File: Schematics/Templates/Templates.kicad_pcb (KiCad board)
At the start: 4 copper layers, 48 x 48 mm, 2 parts, among them J1 Stack Male Edge Connector, U1 SAM-M8Q

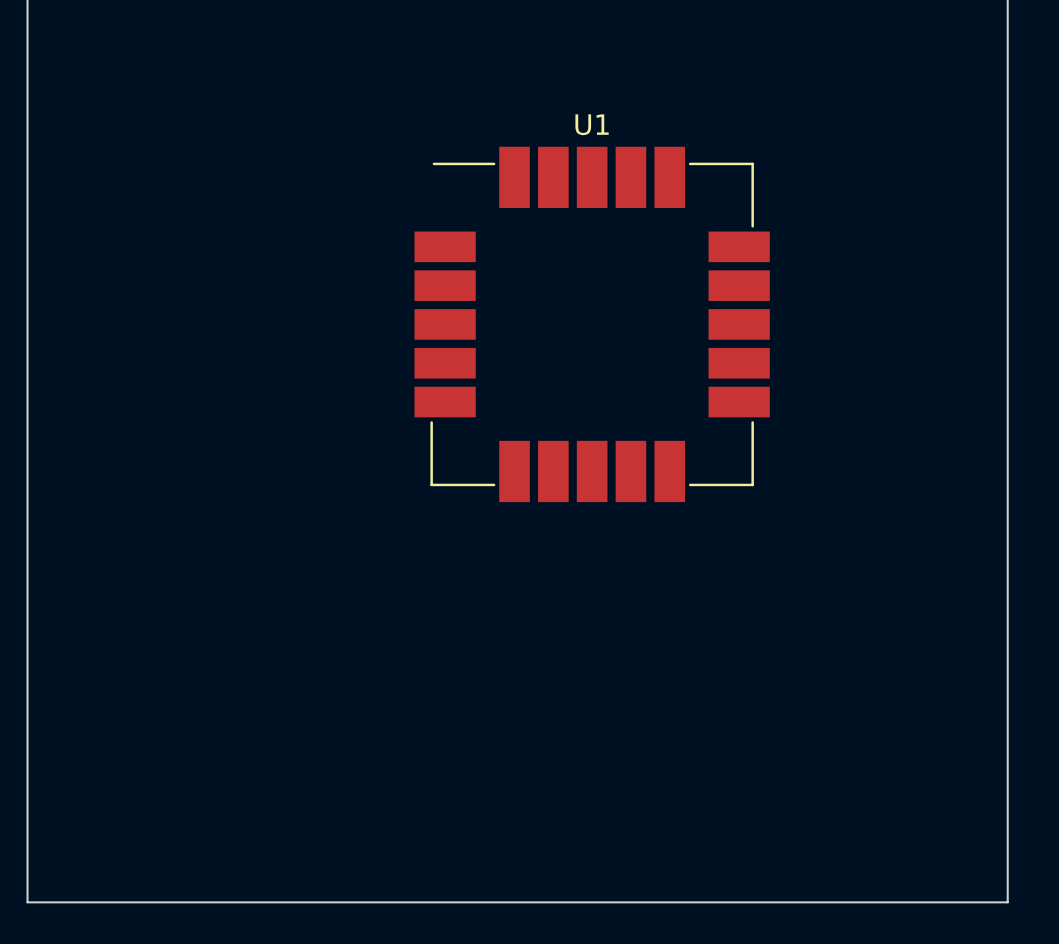
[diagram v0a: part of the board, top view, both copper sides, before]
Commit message: Added SWD programming header
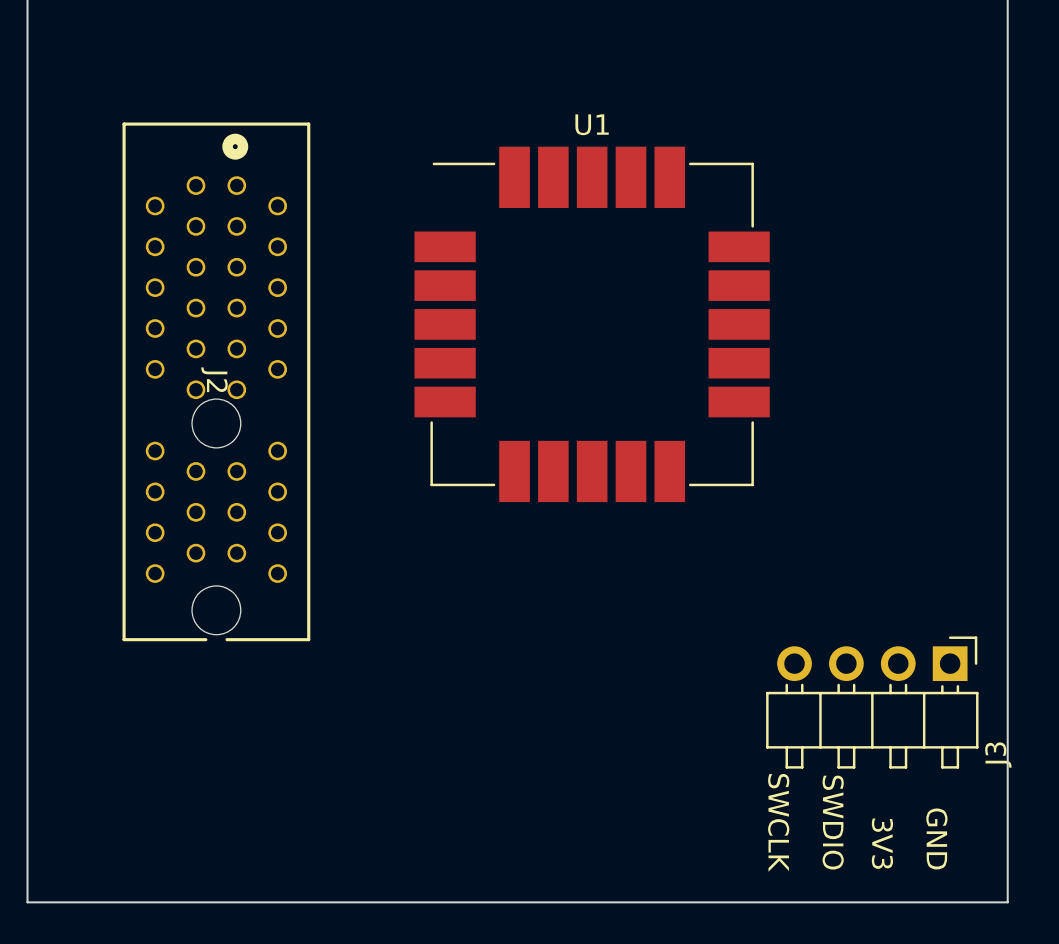
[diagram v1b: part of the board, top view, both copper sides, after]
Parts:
- added J2: Stack Female Edge Connector, footprints:CONN_10018784_AMP, F.Cu at (196.2, 101.5)
- added J3: SWD_01x04_Pin, SWD_Header:SWD_PinHeader_1x04_P2.54mm_Horizontal, F.Cu at (231.1, 124.9)
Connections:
- J1 pad A1: unconnected-(J1-~{PRSNT1}-PadA1) -> Net-(J1-BATT_A-PadA1)
- J1 pad A10: Net-(J1-+3.3V-PadA10) -> Net-(J1-BATT_B-PadA10)
- J1 pad A11: unconnected-(J1-~{PERST}-PadA11) -> Net-(J1-GND_B-PadA11)
- J1 pad A12: unconnected-(J1-GND-PadA12) -> Net-(J1-GND_B-PadA11)
- J1 pad A13: unconnected-(J1-REFCLK+-PadA13) -> Net-(J1-3.3V_B-PadA13)
- J1 pad A14: unconnected-(J1-REFCLK--PadA14) -> Net-(J1-GND_B-PadA11)
- J1 pad A15: unconnected-(J1-GND-PadA12) -> unconnected-(J1-CAN_H-PadA15)
- J1 pad A18: unconnected-(J1-GND-PadA12) -> unconnected-(J1-Reserved-PadA18)
- J1 pad A2: Net-(J1-+12V-PadA2) -> Net-(J1-BATT_A-PadA1)
- J1 pad A3: Net-(J1-+12V-PadA2) -> Net-(J1-GND_A-PadA3)
- J1 pad A4: unconnected-(J1-GND-PadA12) -> Net-(J1-GND_A-PadA3)
- J1 pad A5: unconnected-(J1-JTAG2-PadA5) -> Net-(J1-3.3V_A-PadA5)
- J1 pad A6: unconnected-(J1-JTAG3-PadA6) -> Net-(J1-GND_A-PadA3)
- J1 pad A7: unconnected-(J1-JTAG4-PadA7) -> Net-(J1-5.0V_A-PadA7)
- J1 pad A8: unconnected-(J1-JTAG5-PadA8) -> Net-(J1-GND_A-PadA3)
- J1 pad A9: Net-(J1-+3.3V-PadA10) -> Net-(J1-BATT_B-PadA10)
- J1 pad B1: Net-(J1-+12V-PadA2) -> Net-(J1-BATT_A-PadA1)
- J1 pad B10: unconnected-(J1-3.3Vaux-PadB10) -> Net-(J1-BATT_B-PadA10)
- J1 pad B11: unconnected-(J1-~{WAKE}-PadB11) -> Net-(J1-GND_B-PadA11)
- J1 pad B12: unconnected-(J1-RSVD-PadB12) -> Net-(J1-GND_B-PadA11)
- J1 pad B13: unconnected-(J1-GND-PadA12) -> Net-(J1-3.3V_B-PadA13)
- J1 pad B14: unconnected-(J1-PETp0-PadB14) -> Net-(J1-GND_B-PadA11)
- J1 pad B16: unconnected-(J1-GND-PadA12) -> unconnected-(J1-Reserved-PadB16)
- J1 pad B18: unconnected-(J1-GND-PadA12) -> unconnected-(J1-Reserved-PadB18)
- J1 pad B2: Net-(J1-+12V-PadA2) -> Net-(J1-BATT_A-PadA1)
- J1 pad B3: Net-(J1-+12V-PadA2) -> Net-(J1-GND_A-PadA3)
- J1 pad B4: unconnected-(J1-GND-PadA12) -> Net-(J1-GND_A-PadA3)
- J1 pad B5: unconnected-(J1-SMCLK-PadB5) -> Net-(J1-3.3V_A-PadA5)
- J1 pad B6: unconnected-(J1-SMDAT-PadB6) -> Net-(J1-GND_A-PadA3)
- J1 pad B7: unconnected-(J1-GND-PadA12) -> Net-(J1-5.0V_A-PadA7)
- J1 pad B8: Net-(J1-+3.3V-PadA10) -> Net-(J1-GND_A-PadA3)
- J1 pad B9: unconnected-(J1-JTAG1-PadB9) -> Net-(J1-BATT_B-PadA10)

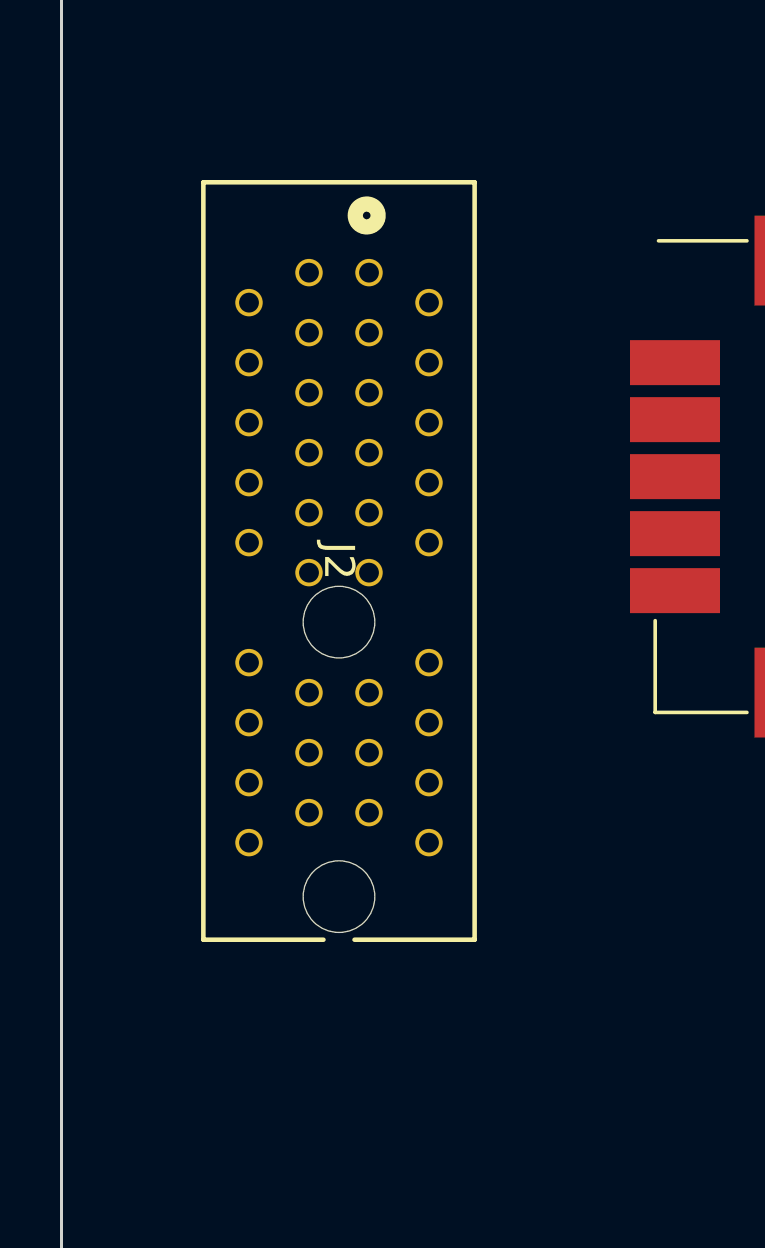
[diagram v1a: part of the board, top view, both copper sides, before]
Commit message: Updated female edge connector footprint & model
Switched to the 10018784-10210TLF PCIe 1x female connector. Updated footprint appropriately, and added 3D model.
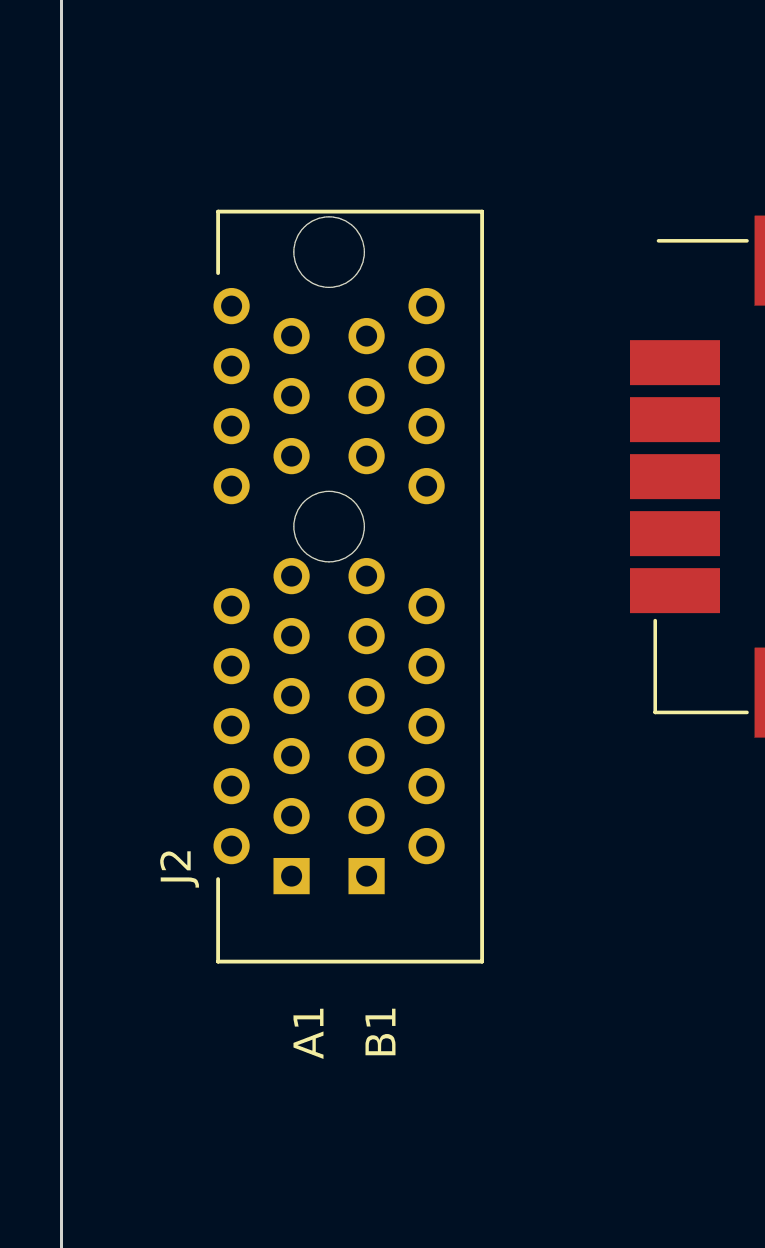
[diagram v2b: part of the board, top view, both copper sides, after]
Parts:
- J2: footprint footprints:CONN_10018784_AMP -> footprints:AMPHENOL_10018784-10210TLF
- moved J2 8.57 mm to (194.9, 110.0), turned to 90 degrees

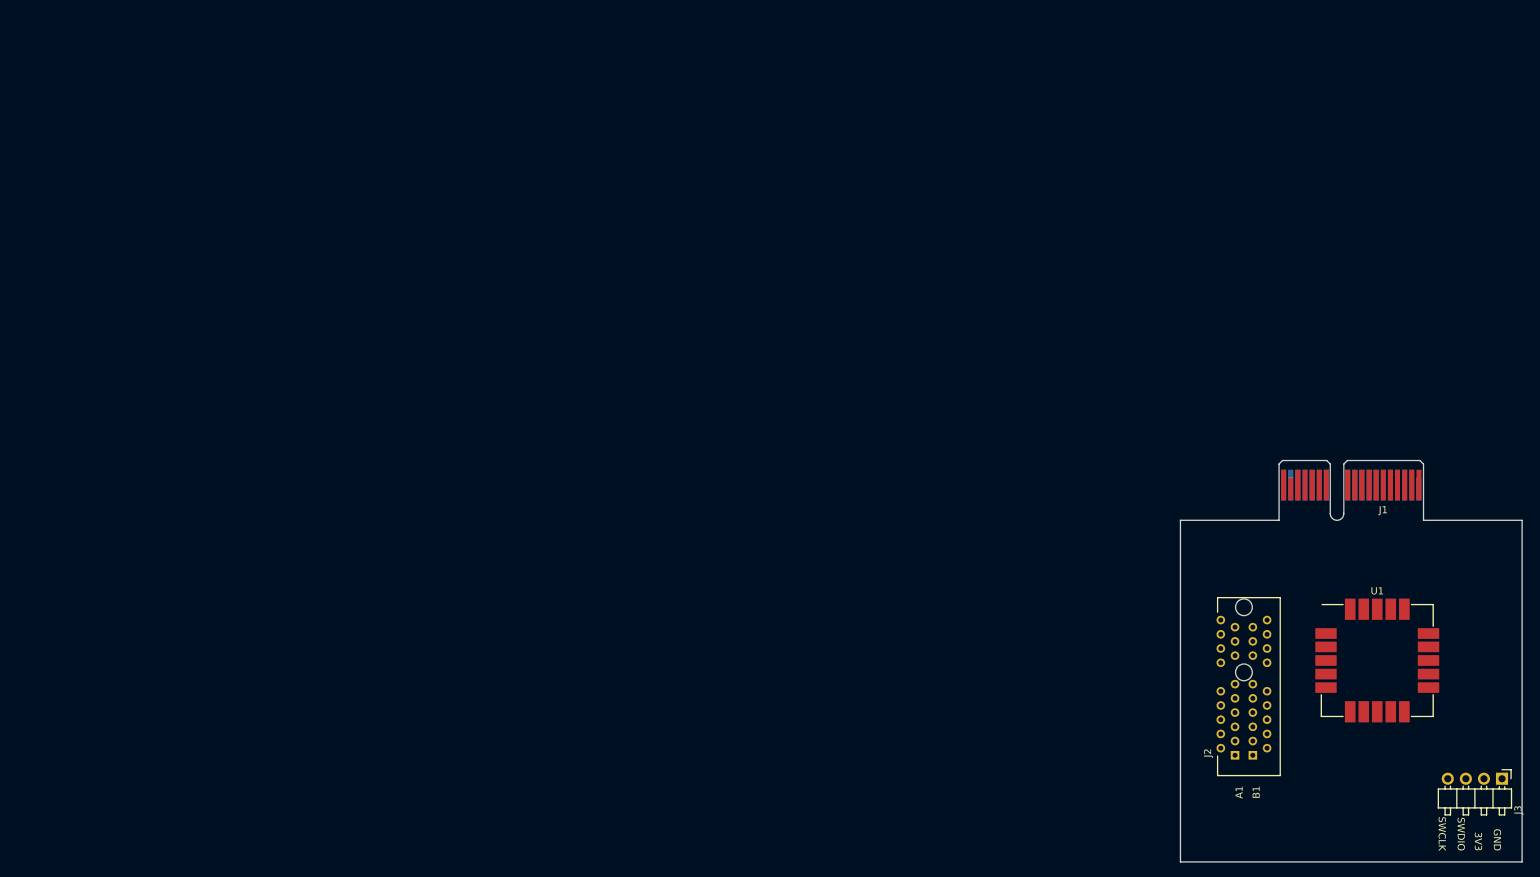
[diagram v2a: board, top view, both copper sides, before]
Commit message: Updated PCB Template
Adjusted PCB project settings & updated PCB board outline
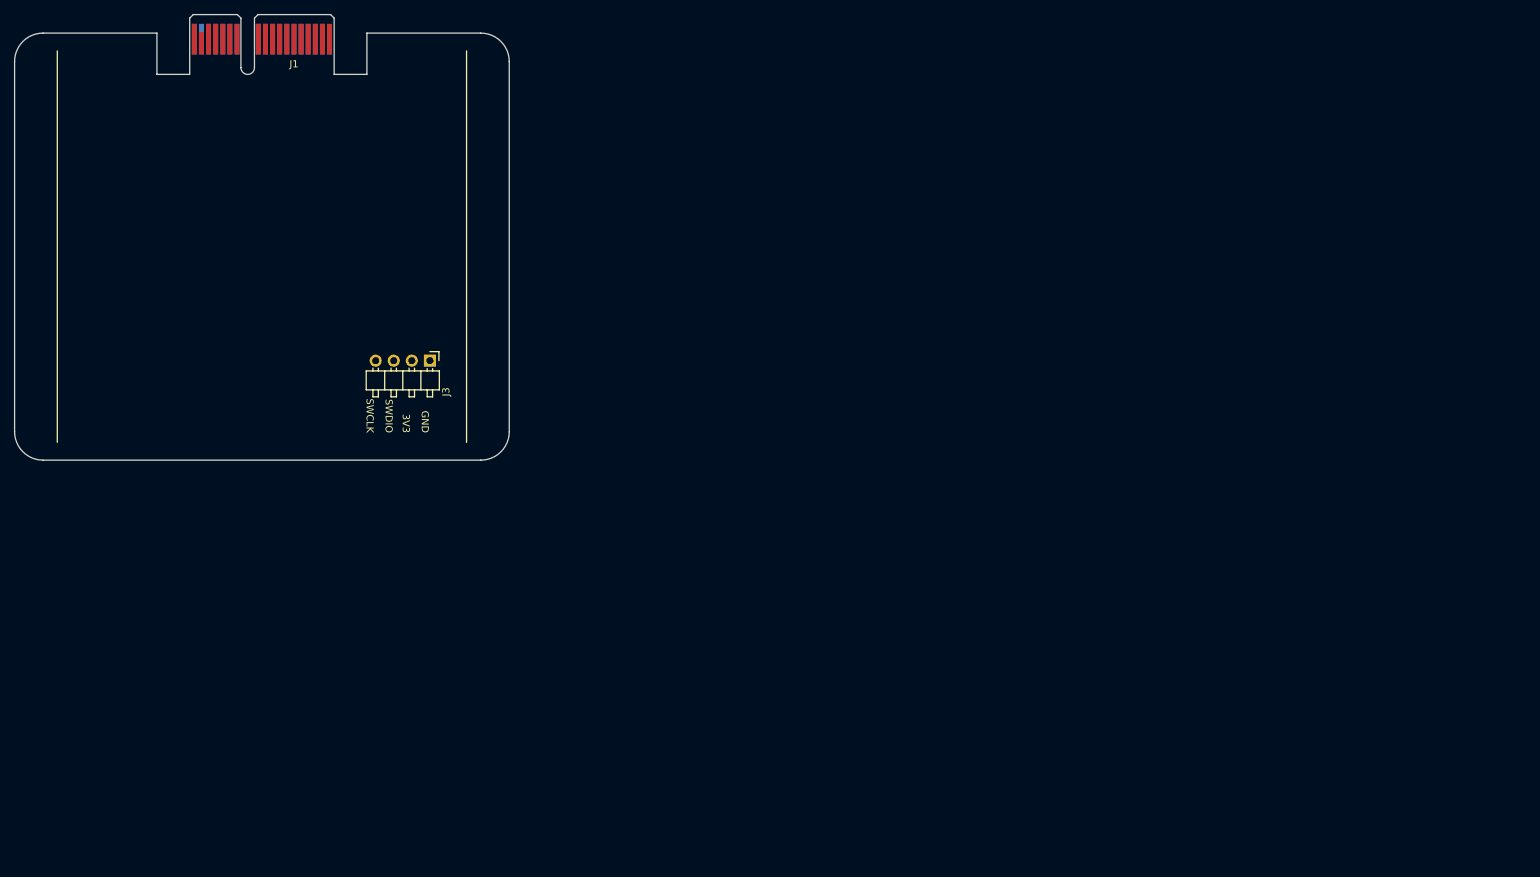
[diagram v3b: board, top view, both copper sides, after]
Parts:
- removed J2: Stack Female Edge Connector, footprints:AMPHENOL_10018784-10210TLF
- removed U1: SAM-M8Q, RF_GPS:ublox_SAM-M8Q_HandSolder
- moved J1 165.4 mm to (66.4, 21.0)
- moved J3 161.7 mm to (80.5, 66.2)
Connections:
- J3 pad 1: unconnected-(J3-GND-Pad1) -> GND
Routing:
- added copper zone on In1.Cu, net GND
- added copper zone on In2.Cu, net GND
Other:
- board size 48 x 48 mm -> 69.5 x 60 mm

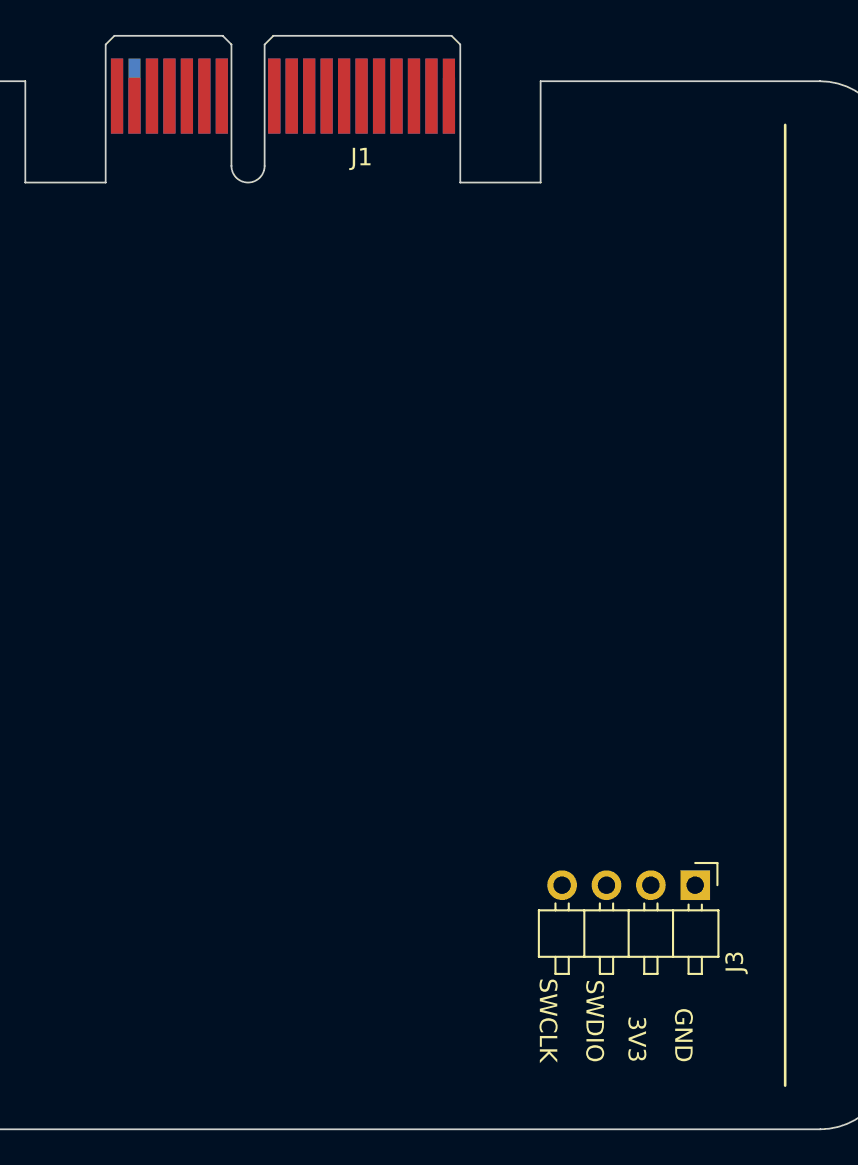
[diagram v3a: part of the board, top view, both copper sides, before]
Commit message: Removed keepout at front of PCB template
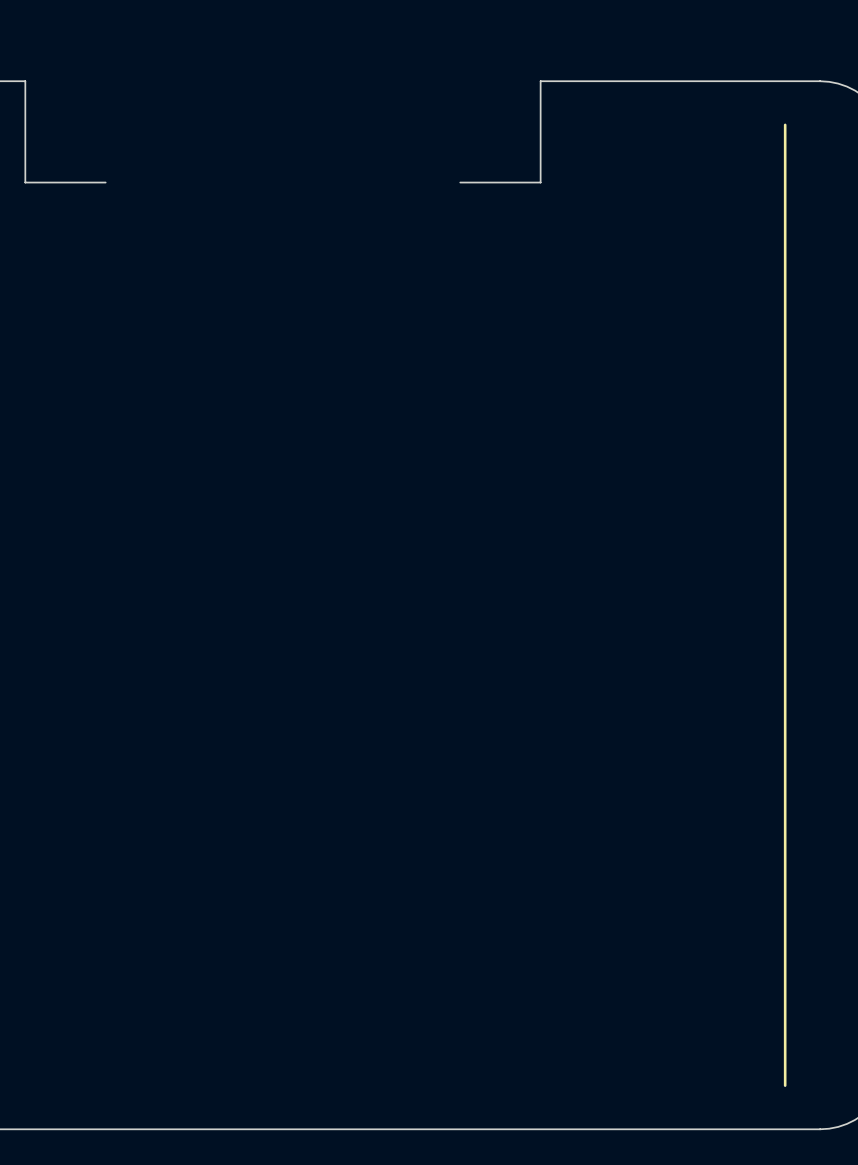
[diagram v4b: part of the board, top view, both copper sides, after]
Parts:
- removed J1: Stack Male Edge Connector, Connector_PCBEdge:BUS_PCIexpress_x1
- removed J3: SWD_01x04_Pin, SWD_Header:SWD_PinHeader_1x04_P2.54mm_Horizontal
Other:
- board text added: "USE GRID THAT IS SOME MULTIPLE OF 0.1mm (0.1mm, 0.2mm, 0.5mm, 1.0mm, etc)"
